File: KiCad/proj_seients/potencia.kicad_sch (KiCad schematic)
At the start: 33 parts, among them J1 BATERIA 12V, J4 Motor, J5 Motor, J6 Motor, J7 Manta_Asiento, Q1 IRLZ44N, U2 LM2596S-5, U3 LM1117DT-3.3, U5 PCA9685BS, U6 DRV8871DDA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

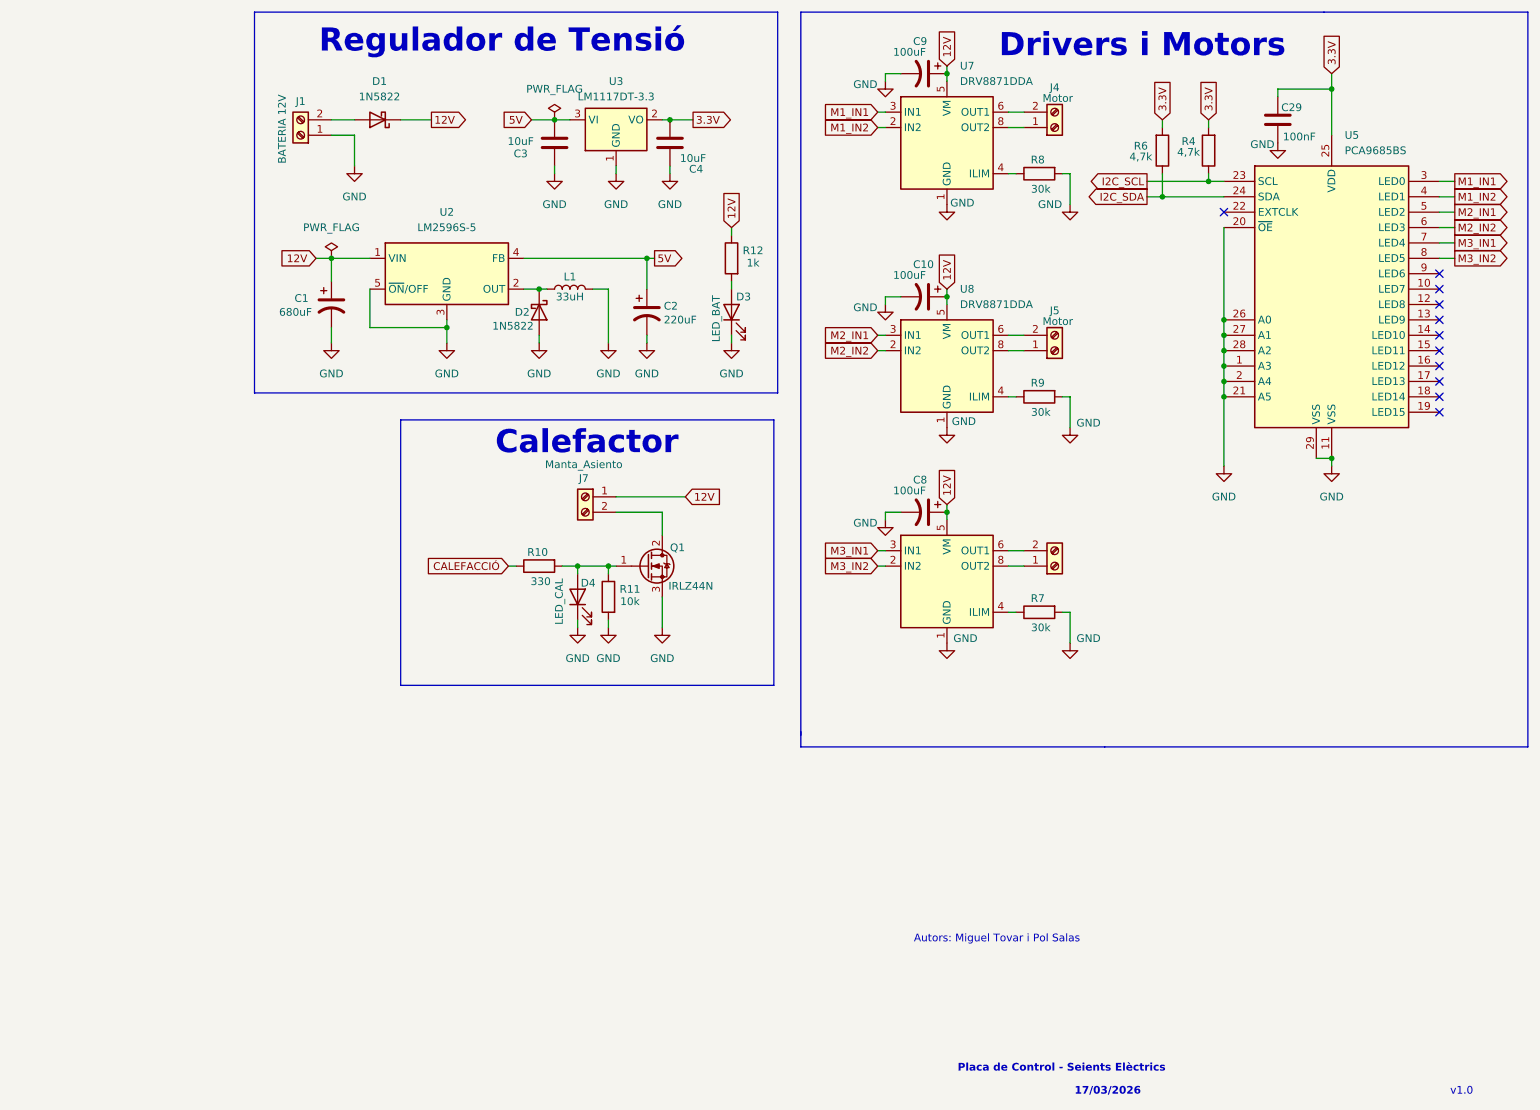
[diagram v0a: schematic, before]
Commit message: Canvi de TCAN i Afegit CAN DE.9
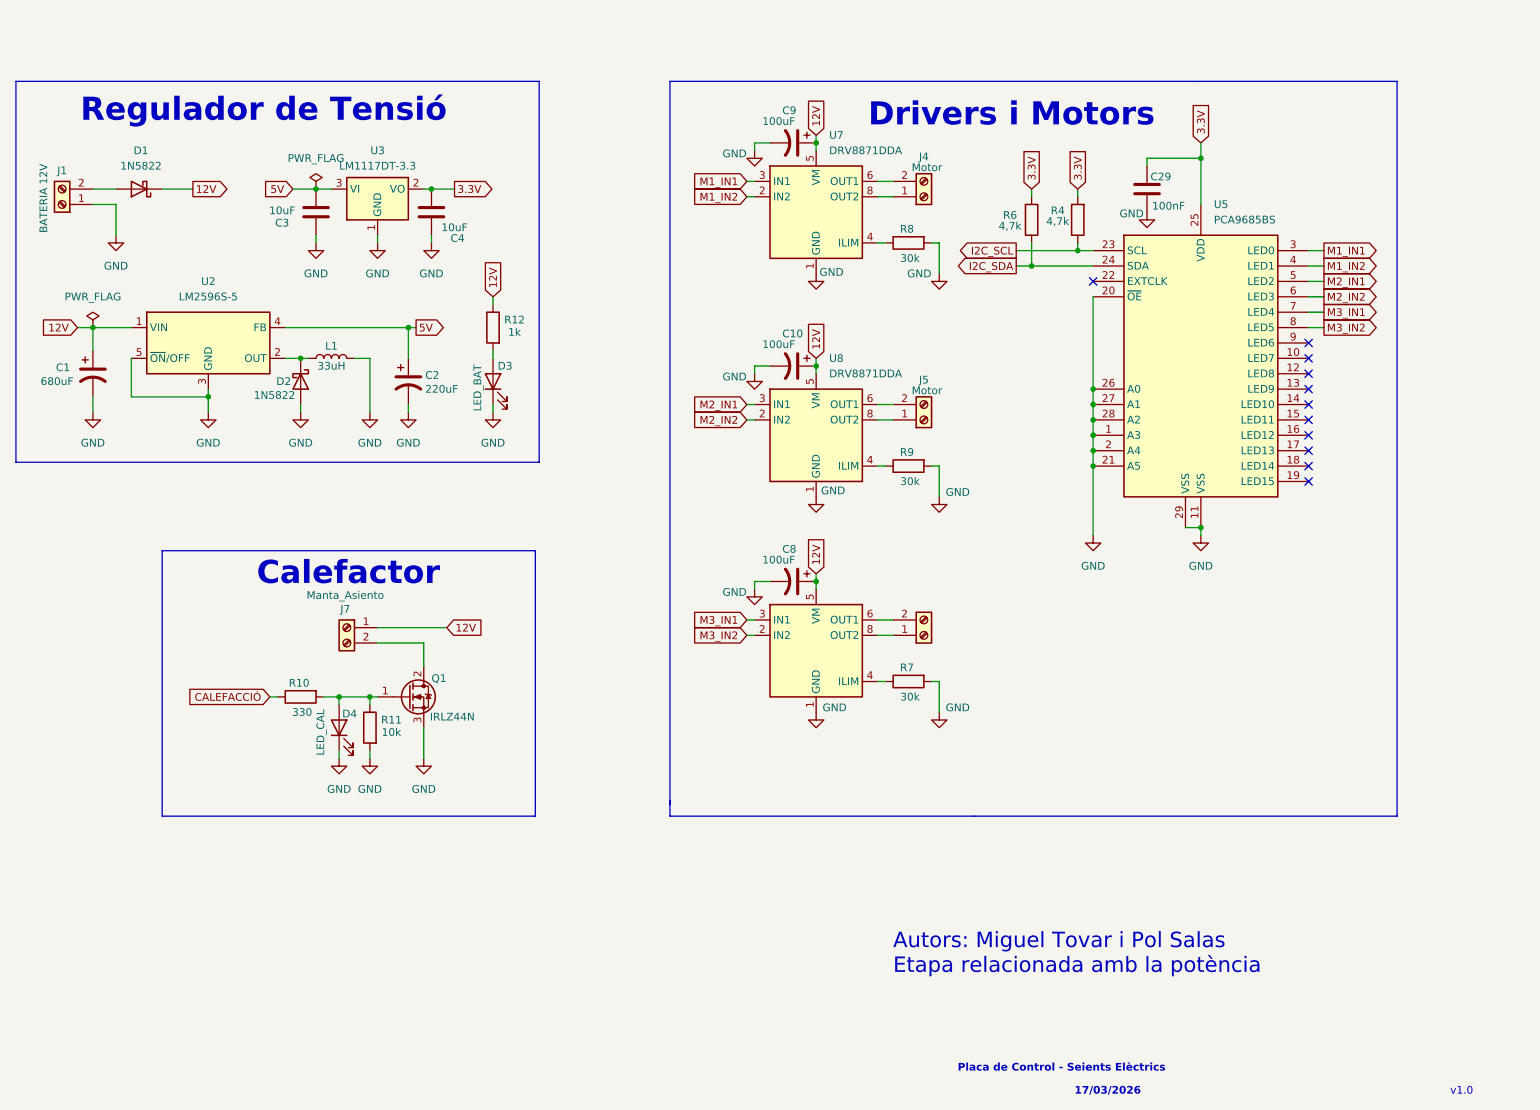
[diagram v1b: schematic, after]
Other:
- note added: "Autors: Miguel Tovar i Pol Salas Etapa relacionada amb la potència"
- note removed: "Autors: Miguel Tovar i Pol Salas"
- moved on the sheet: C1, C10, C2, C29, C3, C4, C8, C9, D1, D2, D3, D4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

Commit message: Canvis de pulsadors, estètica dels drivers i commentaris extres
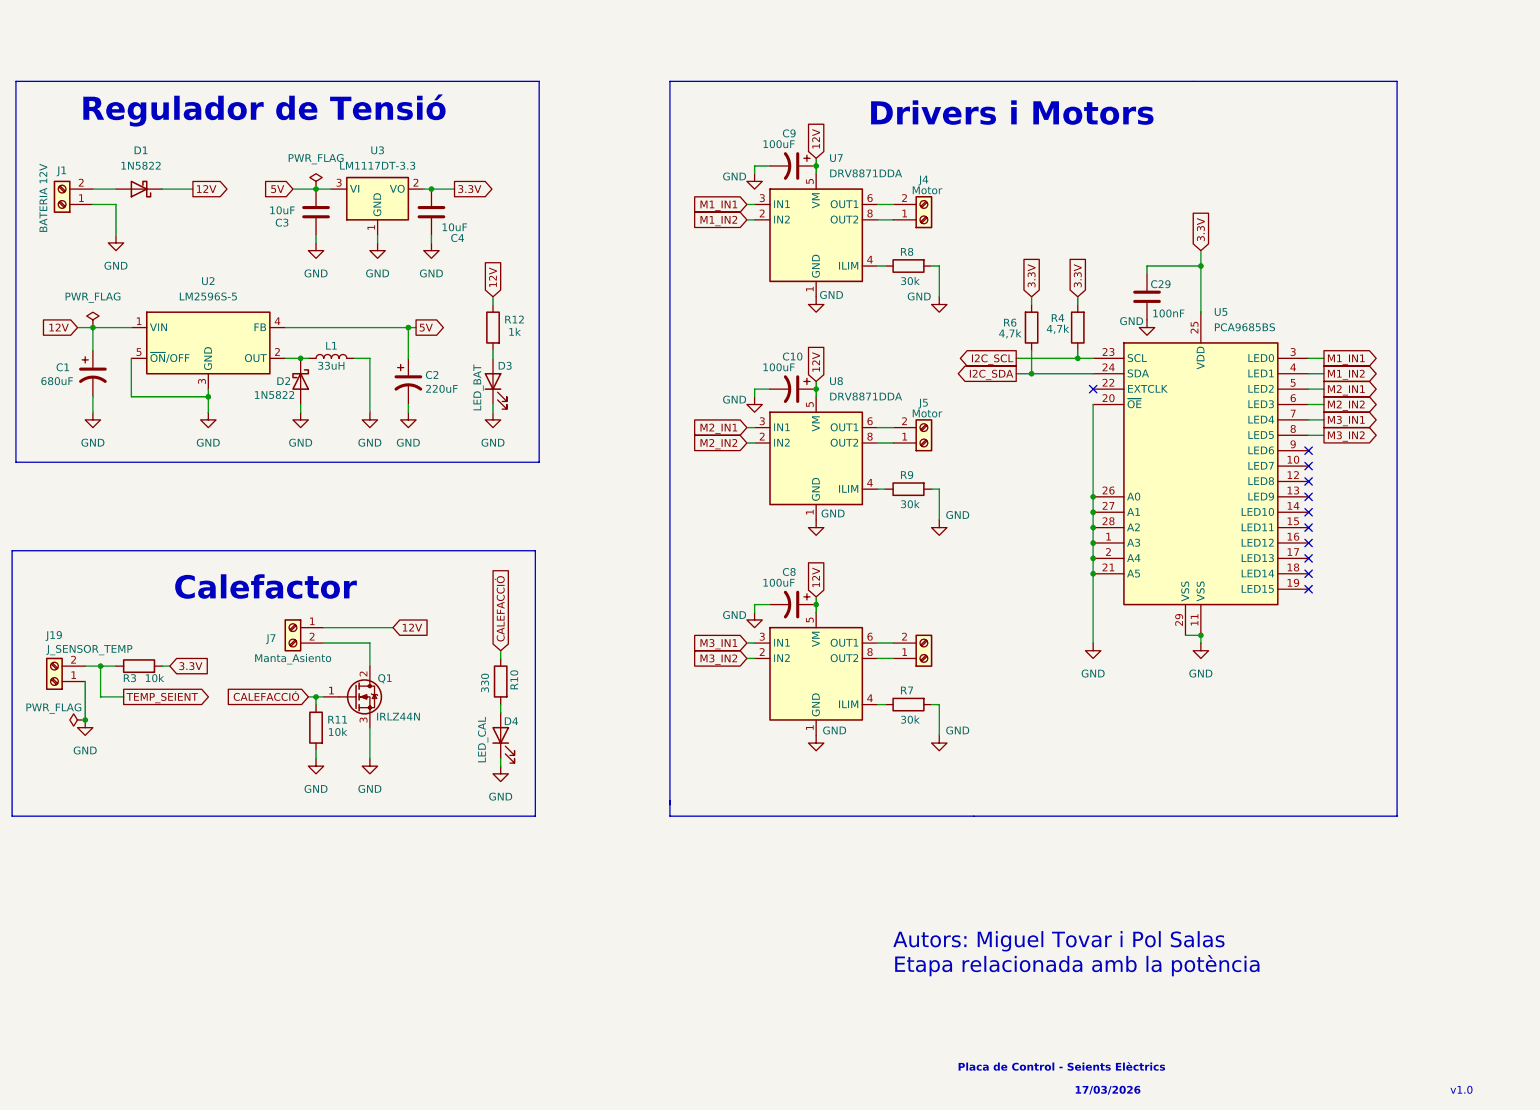
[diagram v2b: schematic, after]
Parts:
- added J19: J_SENSOR_TEMP, symbol Connector:Screw_Terminal_01x02
- added R3: 10k, symbol Device:R
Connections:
- net 3.3V: now also R3.2
- net CALEFACCIÓ: now also Q1.1 (G), R11.1
- net GND: now also J19.1 (Pin_1)
- net at D4.2 (A), R10.2: no longer Q1.1 (G), R11.1
- new net TEMP_SEIENT: J19.2 (Pin_2), R3.1
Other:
- moved on the sheet: C10, C29, C8, C9, D4, J4, J5, J7, Q1, R10, R11, R4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

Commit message: Huellas agefides
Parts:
- C1: footprint (none) -> Capacitor_THT:CP_Radial_D10.0mm_P5.00mm
- C10, C2, C8, C9: footprint (none) -> Capacitor_THT:CP_Radial_D8.0mm_P3.50mm
- C29, C3, C4: footprint (none) -> Capacitor_SMD:C_0805_2012Metric
- D3, D4: footprint (none) -> LED_SMD:LED_0805_2012Metric
- J1, J19, J4, J5, J6, J7: footprint (none) -> TerminalBlock_Phoenix:TerminalBlock_Phoenix_MKDS-1,5-2-5.08_1x02_P5.08mm_Horizontal
- L1: footprint (none) -> Inductor_THT:L_Radial_D10.0mm_P5.00mm_Fastron_07M
- R10, R11, R12, R3, R4, R6, R7, R8, R9: footprint (none) -> Resistor_SMD:R_0805_2012Metric
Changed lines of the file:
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@@
 			)
 		)
-		(property "Footprint" ""
+		(property "Footprint" "Capacitor_THT:CP_Radial_D10.0mm_P5.00mm"
 			(at 45.72 74.93 0)
 			(effects
@@
 			)
 		)
-		(property "Footprint" ""
+		(property "Footprint" "Resistor_SMD:R_0805_2012Metric"
 			(at 53.34 124.968 90)
 			(effects
@@
 			)
 		)
-		(property "Footprint" ""
+		(property "Footprint" "Resistor_SMD:R_0805_2012Metric"
 			(at 113.538 67.31 90)
 			(effects
@@
 			)
 		)
-		(property "Footprint" ""
+		(property "Footprint" "Capacitor_SMD:C_0805_2012Metric"
 			(at 100.6348 44.45 0)
 			(effects
@@
 			)
 		)
-		(property "Footprint" ""
+		(property "Footprint" "TerminalBlock_Phoenix:TerminalBlock_Phoenix_MKDS-1,5-2-5.08_1x02_P5.08mm_Horizontal"
 			(at 39.37 125.73 0)
 			(effects
@@
 			)
 		)
-		(property "Footprint" ""
+		(property "Footprint" "Capacitor_THT:CP_Radial_D8.0mm_P3.50mm"
 			(at 161.29 40.64 0)
 			(effects
@@
 			)
 		)
-		(property "Footprint" ""
+		(property "Footprint" "Resistor_SMD:R_0805_2012Metric"
 			(at 210.058 67.31 90)
 			(effects
@@
 			)
 		)
-		(property "Footprint" ""
+		(property "Footprint" "Inductor_THT:L_Radial_D10.0mm_P5.00mm_Fastron_07M"
 			(at 85.09 72.39 0)
 			(effects
@@
 			)
 		)
-		(property "Footprint" ""
+		(property "Footprint" "TerminalBlock_Phoenix:TerminalBlock_Phoenix_MKDS-1,5-2-5.08_1x02_P5.08mm_Horizontal"
 			(at 182.88 121.92 0)
 			(effects
@@
 			)
 		)
-		(property "Footprint" ""
+		(property "Footprint" "TerminalBlock_Phoenix:TerminalBlock_Phoenix_MKDS-1,5-2-5.08_1x02_P5.08mm_Horizontal"
 			(at 182.88 86.36 0)
 			(effects
@@
 			)
 		)
-		(property "Footprint" ""
+		(property "Footprint" "Resistor_SMD:R_0805_2012Metric"
 			(at 198.882 67.31 90)
 			(effects
@@
 		(exclude_from_sim no)
 		(in_bom yes)
-		(on_board yes)
+		(on_board no)
 		(dnp no)
 		(property "Reference" "J7"
@@
 			)
 		)
-		(property "Footprint" ""
+		(property "Footprint" "TerminalBlock_Phoenix:TerminalBlock_Phoenix_MKDS-1,5-2-5.08_1x02_P5.08mm_Horizontal"
 			(at 78.74 116.84 0)
 			(effects
@@
 			)
 		)
-		(property "Footprint" ""
+		(property "Footprint" "Resistor_SMD:R_0805_2012Metric"
 			(at 180.34 127.762 90)
 			(effects
@@
 			)
 		)
-		(property "Footprint" ""
+		(property "Footprint" "Resistor_SMD:R_0805_2012Metric"
 			(at 180.34 55.372 90)
 			(effects
@@
 			)
 		)
-		(property "Footprint" ""
+		(property "Footprint" "Resistor_SMD:R_0805_2012Metric"
 			(at 114.808 125.73 90)
 			(effects
@@
 			)
 		)
-		(property "Footprint" ""
+		(property "Footprint" "Resistor_SMD:R_0805_2012Metric"
 			(at 180.34 92.202 90)
 			(effects
@@
 			)
 		)
-		(property "Footprint" ""
+		(property "Footprint" "LED_SMD:LED_0805_2012Metric"
 			(at 113.03 134.62 0)
 			(effects
@@
 			)
 		)
-		(property "Footprint" ""
+		(property "Footprint" "Capacitor_SMD:C_0805_2012Metric"
 			(at 81.5848 44.45 0)
 			(effects
@@
 	(symbol
 		(lib_id "power:GND")
-		(at 44.45 132.08 0)
+		(at 82.55 138.43 0)
 		(unit 1)
 		(exclude_from_sim no)
@@
 		(dnp no)
 		(fields_autoplaced yes)
-		(property "Reference" "#PWR0101"
-			(at 44.45 138.43 0)
+		(property "Reference" "#PWR029"
+			(at 82.55 144.78 0)
 			(effects
 				(font
@@
 		)
 		(property "Value" "GND"
-			(at 44.45 137.16 0)
+			(at 82.55 143.51 0)
 			(effects
 				(font
@@
 		)
 		(property "Footprint" ""
-			(at 44.45 132.08 0)
+			(at 82.55 138.43 0)
 			(effects
 				(font
@@
 		)
 		(property "Datasheet" ""
-			(at 44.45 132.08 0)
+			(at 82.55 138.43 0)
 			(effects
 				(font
@@
 		)
 		(property "Description" "Power symbol creates a global label with name \"GND\" , ground"
-			(at 44.45 132.08 0)
+			(at 82.55 138.43 0)
 			(effects
 				(font
@@
 			(project "proj_seients"
 				(path "/abdea21b-3040-408b-b009-221f8b614884/4a4282cf-dc92-46de-ac55-98ec74b7bb09"
-					(reference "#PWR0101")
+					(reference "#PWR029")
+					(unit 1)
+				)
+			)
+			(project "potencia"
+				(path "/e703235d-88cc-45b4-9841-d784390bc6ab"
+					(reference "#PWR?")
 					(unit 1)
 				)
@@
 	(symbol
 		(lib_id "power:GND")
-		(at 82.55 138.43 0)
+		(at 44.45 132.08 0)
 		(unit 1)
 		(exclude_from_sim no)
@@
 		(dnp no)
 		(fields_autoplaced yes)
-		(property "Reference" "#PWR029"
-			(at 82.55 144.78 0)
+		(property "Reference" "#PWR0101"
+			(at 44.45 138.43 0)
 			(effects
 				(font
@@
 		)
 		(property "Value" "GND"
-			(at 82.55 143.51 0)
+			(at 44.45 137.16 0)
 			(effects
 				(font
@@
 		)
 		(property "Footprint" ""
-			(at 82.55 138.43 0)
+			(at 44.45 132.08 0)
 			(effects
 				(font
@@
 		)
 		(property "Datasheet" ""
-			(at 82.55 138.43 0)
+			(at 44.45 132.08 0)
 			(effects
 				(font
@@
 		)
 		(property "Description" "Power symbol creates a global label with name \"GND\" , ground"
-			(at 82.55 138.43 0)
+			(at 44.45 132.08 0)
 			(effects
 				(font
@@
 			(project "proj_seients"
 				(path "/abdea21b-3040-408b-b009-221f8b614884/4a4282cf-dc92-46de-ac55-98ec74b7bb09"
-					(reference "#PWR029")
-					(unit 1)
-				)
-			)
-			(project "potencia"
-				(path "/e703235d-88cc-45b4-9841-d784390bc6ab"
-					(reference "#PWR?")
+					(reference "#PWR0101")
 					(unit 1)
 				)
@@
 			)
 		)
-		(property "Footprint" ""
+		(property "Footprint" "TerminalBlock_Phoenix:TerminalBlock_Phoenix_MKDS-1,5-2-5.08_1x02_P5.08mm_Horizontal"
 			(at 40.64 46.99 0)
 			(effects
@@
 			)
 		)
-		(property "Footprint" ""
+		(property "Footprint" "Resistor_SMD:R_0805_2012Metric"
 			(at 84.328 133.35 90)
 			(effects
@@
 			)
 		)
-		(property "Footprint" ""
+		(property "Footprint" "Capacitor_THT:CP_Radial_D8.0mm_P3.50mm"
 			(at 161.29 77.47 0)
 			(effects
@@
 			)
 		)
-		(property "Footprint" ""
+		(property "Footprint" "TerminalBlock_Phoenix:TerminalBlock_Phoenix_MKDS-1,5-2-5.08_1x02_P5.08mm_Horizontal"
 			(at 182.88 49.53 0)
 			(effects
@@
 			)
 		)
-		(property "Footprint" ""
+		(property "Footprint" "Capacitor_THT:CP_Radial_D8.0mm_P3.50mm"
 			(at 161.29 113.03 0)
 			(effects
@@
 			)
 		)
-		(property "Footprint" ""
+		(property "Footprint" "Capacitor_THT:CP_Radial_D8.0mm_P3.50mm"
 			(at 97.79 76.2 0)
 			(effects
@@
 			)
 		)
-		(property "Footprint" ""
+		(property "Footprint" "LED_SMD:LED_0805_2012Metric"
 			(at 111.76 76.2 0)
 			(effects
@@
 			)
 		)
-		(property "Footprint" ""
+		(property "Footprint" "Capacitor_SMD:C_0805_2012Metric"
 			(at 220.6752 58.42 0)
 			(effects

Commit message: Versió 1.0 Layout
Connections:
- net 12V: now also J7.2 (Pin_2); no longer J7.1 (Pin_1)
- net at Q1.2 (D): now also J7.1 (Pin_1); no longer J7.2 (Pin_2)
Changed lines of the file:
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@@
 	(text "Autors: Miguel Tovar i Pol Salas\nEtapa relacionada amb la potència"
 		(exclude_from_sim no)
-		(at 177.8 170.688 0)
+		(at 178.054 176.784 0)
 		(effects
 			(font
@@
 	)
 	(symbol
-		(lib_id "Connector:Screw_Terminal_01x02")
-		(at 78.74 116.84 0)
-		(mirror y)
-		(unit 1)
-		(exclude_from_sim no)
-		(in_bom yes)
-		(on_board no)
-		(dnp no)
-		(property "Reference" "J7"
-			(at 75.184 118.618 0)
-			(effects
-				(font
-					(size 1.27 1.27)
-				)
-			)
-		)
-		(property "Value" "Manta_Asiento"
-			(at 78.74 121.92 0)
-			(effects
-				(font
-					(size 1.27 1.27)
-				)
-			)
-		)
-		(property "Footprint" "TerminalBlock_Phoenix:TerminalBlock_Phoenix_MKDS-1,5-2-5.08_1x02_P5.08mm_Horizontal"
-			(at 78.74 116.84 0)
-			(effects
-				(font
-					(size 1.27 1.27)
-				)
-				(hide yes)
-			)
-		)
-		(property "Datasheet" "~"
-			(at 78.74 116.84 0)
-			(effects
-				(font
-					(size 1.27 1.27)
-				)
-				(hide yes)
-			)
-		)
-		(property "Description" "Generic screw terminal, single row, 01x02, script generated (kicad-library-utils/schlib/autogen/connector/)"
-			(at 78.74 116.84 0)
-			(effects
-				(font
-					(size 1.27 1.27)
-				)
-				(hide yes)
-			)
-		)
-		(pin "2"
-		)
-		(pin "1"
-		)
-		(instances
-			(project "proj_seients"
-				(path "/abdea21b-3040-408b-b009-221f8b614884/4a4282cf-dc92-46de-ac55-98ec74b7bb09"
-					(reference "J7")
-					(unit 1)
-				)
-			)
-			(project "potencia"
-				(path "/e703235d-88cc-45b4-9841-d784390bc6ab"
-					(reference "J?")
-					(unit 1)
-				)
-			)
-		)
-	)
-	(symbol
 		(lib_id "Device:R")
 		(at 180.34 129.54 90)
@@
 					(unit 1)
 				)
+			)
+		)
+	)
+	(symbol
+		(lib_id "Connector:Screw_Terminal_01x02")
+		(at 78.74 119.38 180)
+		(unit 1)
+		(exclude_from_sim no)
+		(in_bom yes)
+		(on_board yes)
+		(dnp no)
+		(property "Reference" "J7"
+			(at 75.692 119.38 0)
+			(effects
+				(font
+					(size 1.27 1.27)
+				)
+			)
+		)
+		(property "Value" "Manta_Asiento"
+			(at 76.962 122.174 0)
+			(effects
+				(font
+					(size 1.27 1.27)
+				)
+			)
+		)
+		(property "Footprint" "TerminalBlock_Phoenix:TerminalBlock_Phoenix_MKDS-1,5-2-5.08_1x02_P5.08mm_Horizontal"
+			(at 78.74 119.38 0)
+			(effects
+				(font
+					(size 1.27 1.27)
+				)
+				(hide yes)
+			)
+		)
+		(property "Datasheet" "~"
+			(at 78.74 119.38 0)
+			(effects
+				(font
+					(size 1.27 1.27)
+				)
+				(hide yes)
+			)
+		)
+		(property "Description" "Generic screw terminal, single row, 01x02, script generated (kicad-library-utils/schlib/autogen/connector/)"
+			(at 78.74 119.38 0)
+			(effects
+				(font
+					(size 1.27 1.27)
+				)
+				(hide yes)
+			)
+		)
+		(pin "2"
+		)
+		(pin "1"
+		)
+		(instances
+			(project "proj_seients"
+				(path "/abdea21b-3040-408b-b009-221f8b614884/4a4282cf-dc92-46de-ac55-98ec74b7bb09"
+					(reference "J7")
+					(unit 1)
+				)
